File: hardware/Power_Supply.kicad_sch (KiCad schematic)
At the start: 72 parts, among them J25 Conn_01x02, J26 Conn_01x02, U26 LTC3122HMSE#PBF, U27 LTC3115IDHD-2#WPBF, U28 NCP1117-3.3_SOT223, U29 NCP1117-12_SOT223, U30 LM2990SX-12

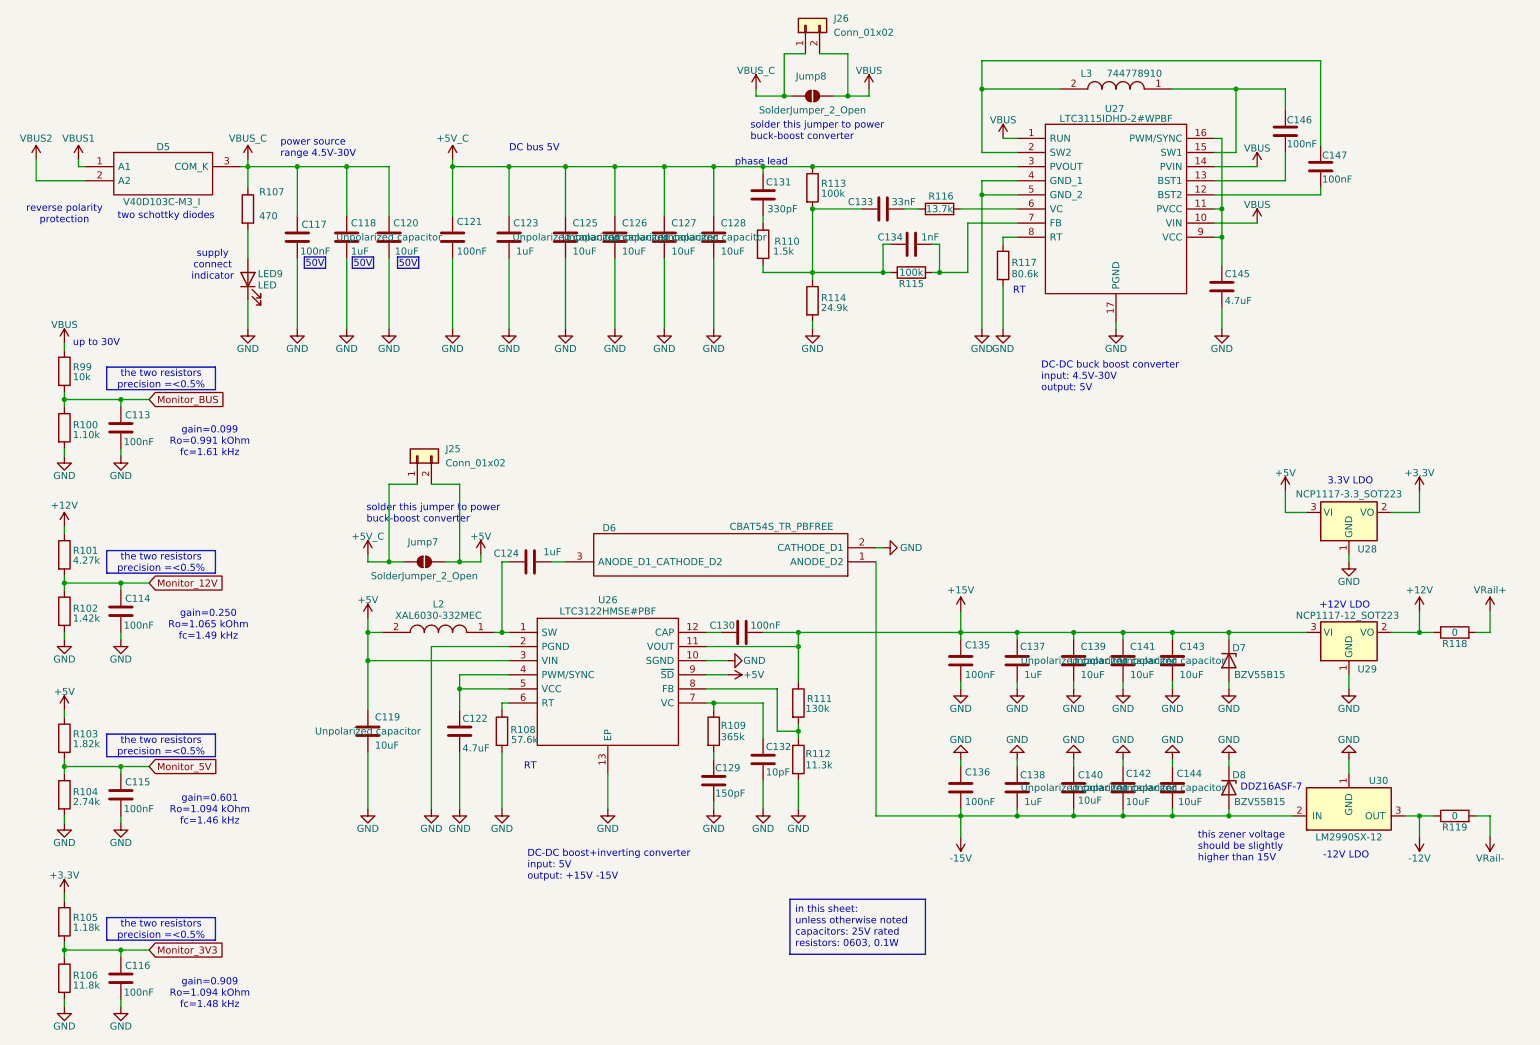
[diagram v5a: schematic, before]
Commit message: Jumpers and interstages connections + added zeners to supply sections + justified text
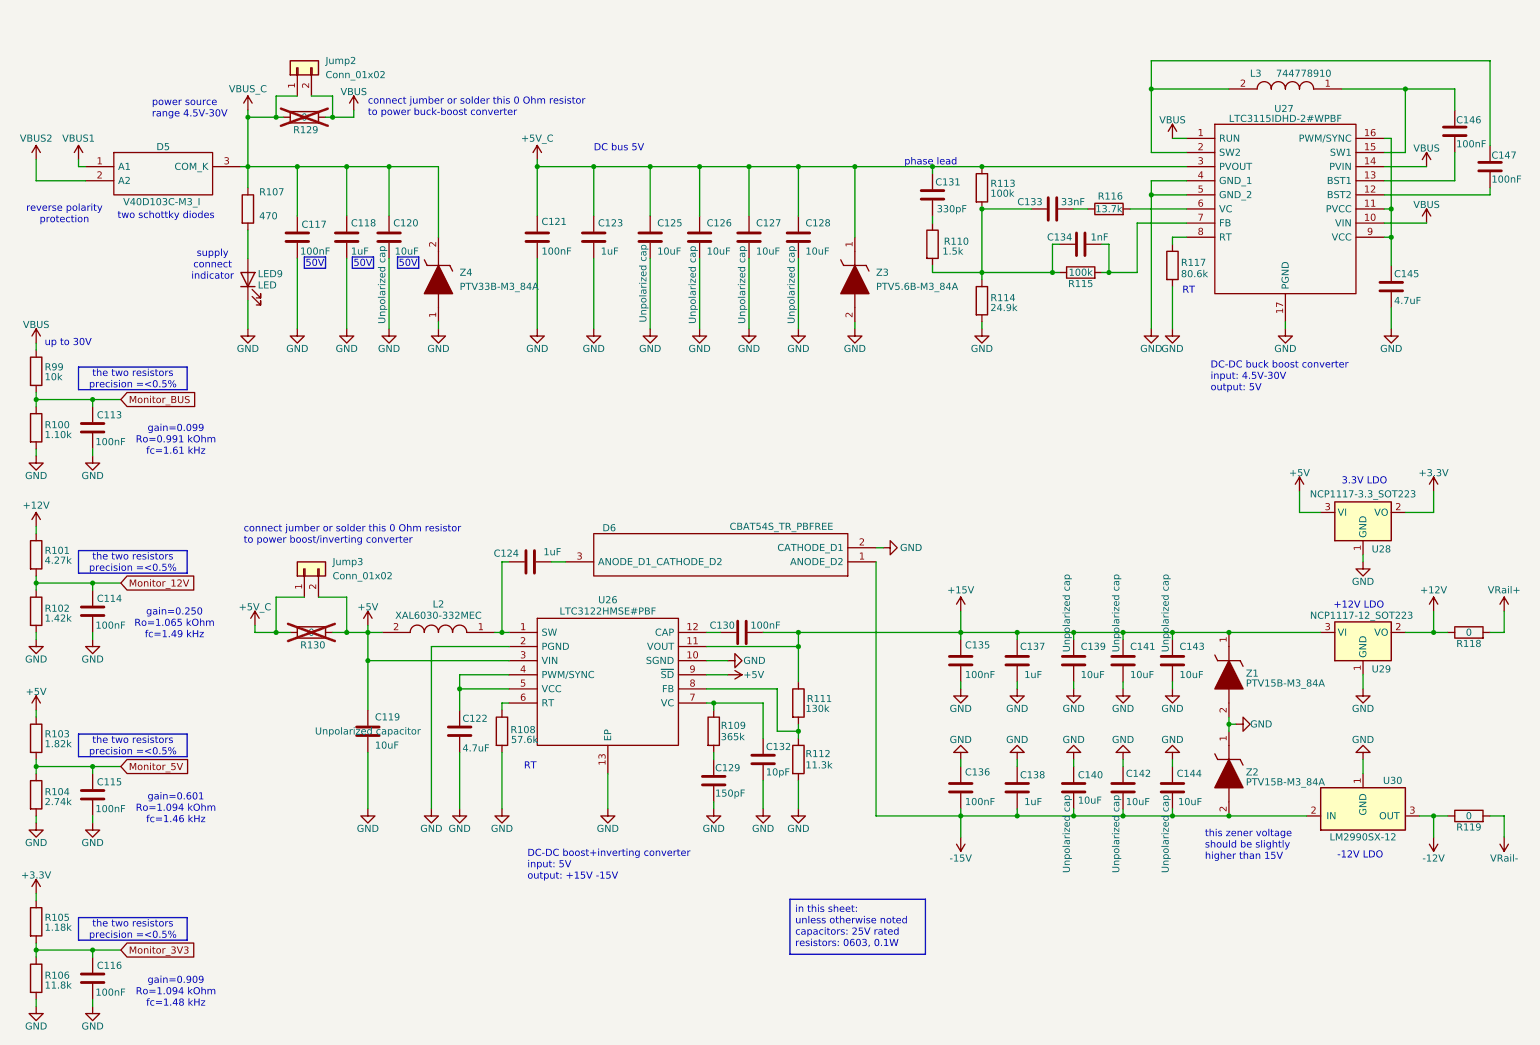
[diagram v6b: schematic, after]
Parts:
- removed D7, D8: BZV55B15, harp.device.quad.dac.kicad:D_MiniMELF, symbol harp.device.quad.dac:BZV55B15
- removed Jump7, Jump8: SolderJumper_2_Open, harp.device.quad.dac.kicad:R_0603_1608Metric_Pad0.98x0.95mm_HandSolder, symbol harp.device.quad.dac:SolderJumper_2_Open
- added R129, R130: 0, Resistor_SMD:R_0603_1608Metric, symbol harp.device.quad.dac:R_0603
- added Z1, Z2: PTV15B-M3_84A, PTV47BM384A, symbol PTV15B-M3_84A:PTV15B-M3_84A
- added Z3: PTV5.6B-M3_84A, PTV56BM384A, symbol PTV5.6B-M3_84A:PTV5.6B-M3_84A
- added Z4: PTV33B-M3_84A, PTV47BM384A, symbol PTV33B-M3_84A:PTV33B-M3_84A
- renumbered J26 to Jump2, J25 to Jump3
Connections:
- net +15V: now also Z1.1
- net +5V: now also R130.2
- net +5V_C: now also R130.1, Z3.1
- net -15V: now also Z2.2
- net GND: now also Z1.2, Z2.1, Z3.2, Z4.1
- net VBUS: now also R129.2
- net VBUS_C: now also R129.1, Z4.2
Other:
- note added: "connect jumber or solder this 0 Ohm resistor to power boost/inverting converter"
- note added: "connect jumber or solder this 0 Ohm resistor to power buck-boost converter"
- note removed: "DDZ16ASF-7"
- note removed: "solder this jumper to power buck-boost converter"
- moved on the sheet: C113, C114, C115, C116, C121, C123, C125, C126, C127, C128, C131, C133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

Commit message: The part designators have been reannotated.
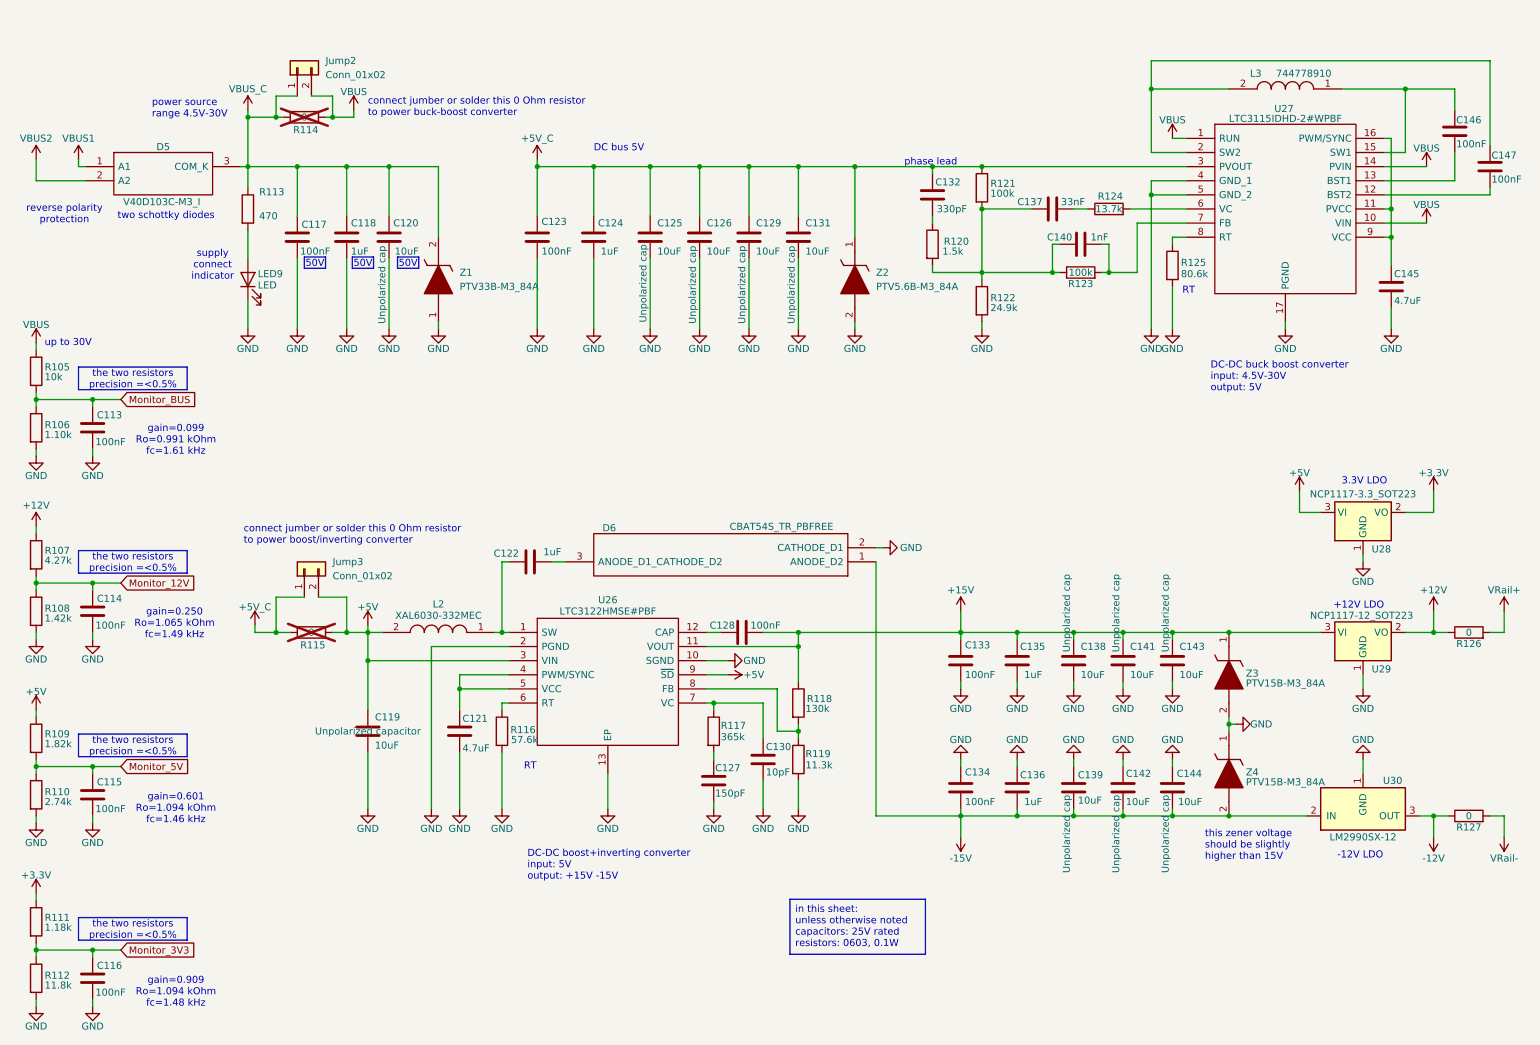
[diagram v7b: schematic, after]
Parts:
- renumbered C122 to C121, C124 to C122, C121 to C123, C123 to C124, C129 to C127, C130 to C128, C127 to C129, C132 to C130, C128 to C131, C131 to C132, C135 to C133, C136 to C134, C137 to C135, C138 to C136, C133 to C137, C139 to C138, C140 to C139, C134 to C140, R99 to R105, R100 to R106, R101 to R107, R102 to R108, R103 to R109, R104 to R110, R105 to R111, R106 to R112, R107 to R113, R129 to R114, R130 to R115, R108 to R116, R109 to R117, R111 to R118, R112 to R119, R110 to R120, R113 to R121, R114 to R122, R115 to R123, R116 to R124, R117 to R125, R118 to R126, R119 to R127, Z4 to Z1, Z3 to Z2, Z1 to Z3, Z2 to Z4
